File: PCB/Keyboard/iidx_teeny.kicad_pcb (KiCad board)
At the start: 2 copper layers, 150 x 100 mm, 46 parts, among them J1 CONN_01x05, SW1 SWITCH_SPST, SW10 SWITCH_SPST, SW11 SWITCH_SPST, SW12 SWITCH_SPST, SW13 SWITCH_SPST, SW2 SWITCH_SPST, SW3 SWITCH_SPST, SW4 SWITCH_SPST, SW5 SWITCH_SPST, SW6 SWITCH_SPST, SW7 SWITCH_SPST, SW8 SWITCH_SPST, SW9 SWITCH_SPST, U1 Pico, U2 SN74LV1T34DBV, U3 SN74LV1T34DBV

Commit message: PCB and keyboard housing done
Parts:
- removed TV1, TV2, TV3: D_TVS, Diode_SMD:D_SOD-323_HandSoldering
- added J2: Conn_01x04, iidx_teeny:Solder_4P, B.Cu at (138.4, 95.9)
- D1: renamed from D10; footprint iidx_pico:WS2812B-2835 -> iidx_teeny:WS2812B-2835
- D2: renamed from D20; footprint iidx_pico:WS2812B-2835 -> iidx_teeny:WS2812B-2835
- D3: renamed from D30; footprint iidx_pico:WS2812B-2835 -> iidx_teeny:WS2812B-2835
- D4: renamed from D40; footprint iidx_pico:WS2812B-2835 -> iidx_teeny:WS2812B-2835
- D5: renamed from D50; footprint iidx_pico:WS2812B-2835 -> iidx_teeny:WS2812B-2835
- D6: renamed from D60; footprint iidx_pico:WS2812B-2835 -> iidx_teeny:WS2812B-2835
- D7: renamed from D70; footprint iidx_pico:WS2812B-2835 -> iidx_teeny:WS2812B-2835
- DA1, DA2, DA3, DA4: footprint iidx_pico:WS2812B-2835 -> iidx_teeny:WS2812B-2835
- J1: value CONN_01x05 -> Conn_01x03; footprint iidx_pico:Pogo_5P_Female -> iidx_teeny:Solder_3P
- SCR1, SCR2, SCR3, SCR4: footprint iidx_pico:MountingHole_3.2mm_M3 -> iidx_teeny:MountingHole_3.2mm_M3
- U2, U3: footprint iidx_pico:SOT-23-5_Jumper -> iidx_teeny:SOT-23-5_Jumper
- moved C2 90.7 mm to (81.1, 127.7)
- moved J1 88.8 mm to (151.9, 95.9), turned to 90 degrees
- moved R3 78.9 mm to (150.9, 89.7), turned to 90 degrees
- moved U3 74.0 mm to (148.4, 89.4), turned to -90 degrees
- moved C5 63.2 mm to (176.9, 127.7)
- moved C3 39.9 mm to (104.9, 127.7)
- moved R20 25.8 mm to (137.1, 79.7)
- moved R21 25.8 mm to (140.1, 79.7)
- moved C1 18.3 mm to (138.3, 84.2), turned to -90 degrees
- moved R1 18.1 mm to (155.4, 89.7)
- moved C4 11.8 mm to (141.0, 127.7)
- moved U2 9.92 mm to (80.8, 110.9)
- moved R2 6.96 mm to (83.3, 111.2)
- moved DA1 0.50 mm to (83.3, 75.1)
- moved DA2 0.50 mm to (105.3, 75.1)
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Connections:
- J1 pad 1: GND -> +5V
- J1 pad 2: /SDA -> /TT_LED
- J1 pad 3: /SCL -> GND
- U1 pad 36: unconnected-(U1-Pad36) -> /3V3
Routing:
- net +5V: track 0.00 -> 517.4 mm, vias 0 -> 9
- net Net-(SW7-Pad1): track 0.00 -> 96.3 mm
- net /LED8: track 0.00 -> 85.7 mm, vias 0 -> 2
- net Net-(SW13-Pad1): track 0.00 -> 84.5 mm, vias 0 -> 1
- net Net-(SW12-Pad1): track 0.00 -> 81.1 mm, vias 0 -> 1
- net Net-(SW11-Pad1): track 0.00 -> 73.6 mm, vias 0 -> 1
- net Net-(SW6-Pad1): track 0.00 -> 65.6 mm, vias 0 -> 1
- net Net-(SW5-Pad1): track 0.00 -> 65.5 mm
- net /LED7: track 0.00 -> 61.7 mm
- net GND: track 0.00 -> 55.9 mm, vias 0 -> 16
- net /LED3: track 0.00 -> 54.8 mm
- net /LED5: track 0.00 -> 54.8 mm
- net /LED1: track 0.00 -> 54.8 mm
- net Net-(SW10-Pad1): track 0.00 -> 54.0 mm, vias 0 -> 1
- net Net-(SW3-Pad1): track 0.00 -> 53.1 mm
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- added copper zone on B.Cu, net GND
- added copper zone on F.Cu, net GND
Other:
- board text added: "3V C D G"
- board text added: "5V L G"
- board text removed: "G D C L V"

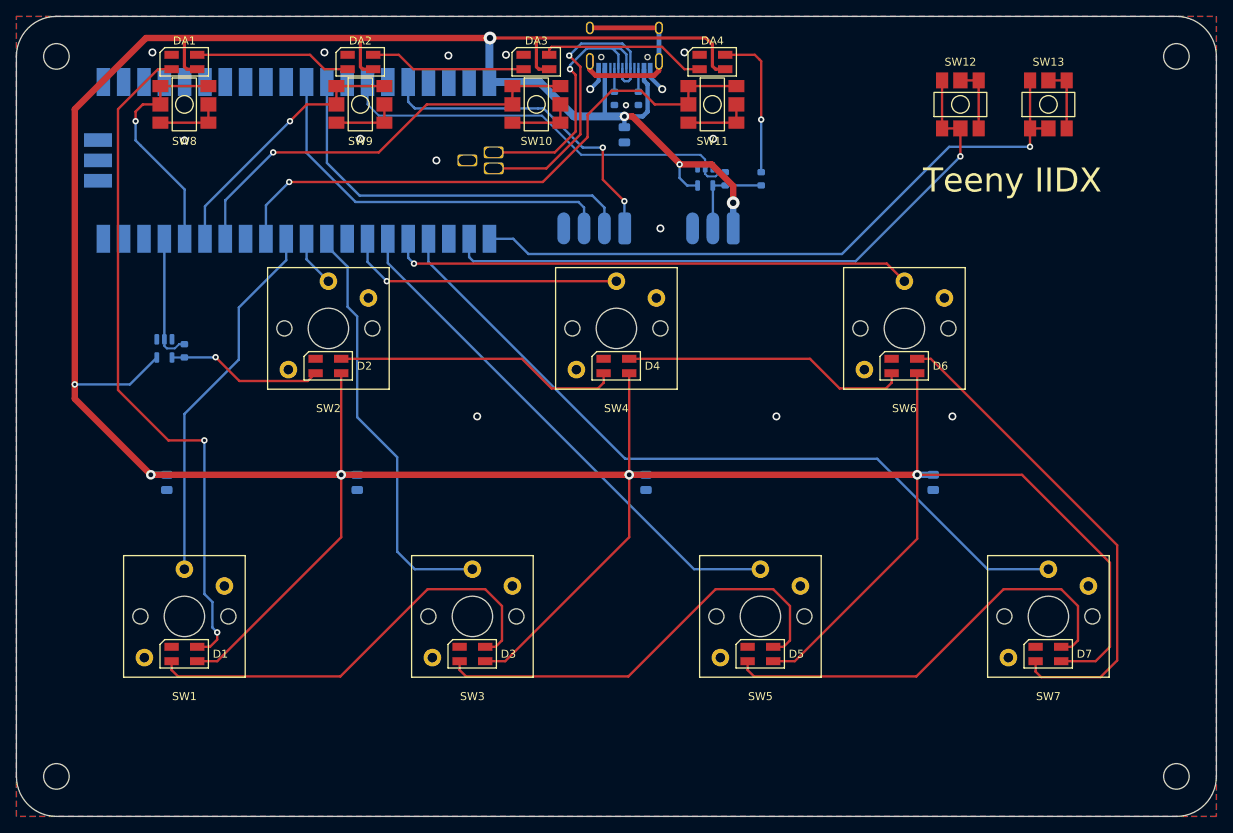
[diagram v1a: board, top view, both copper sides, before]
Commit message: PCB updated with two LEDs per button and larger Y gap
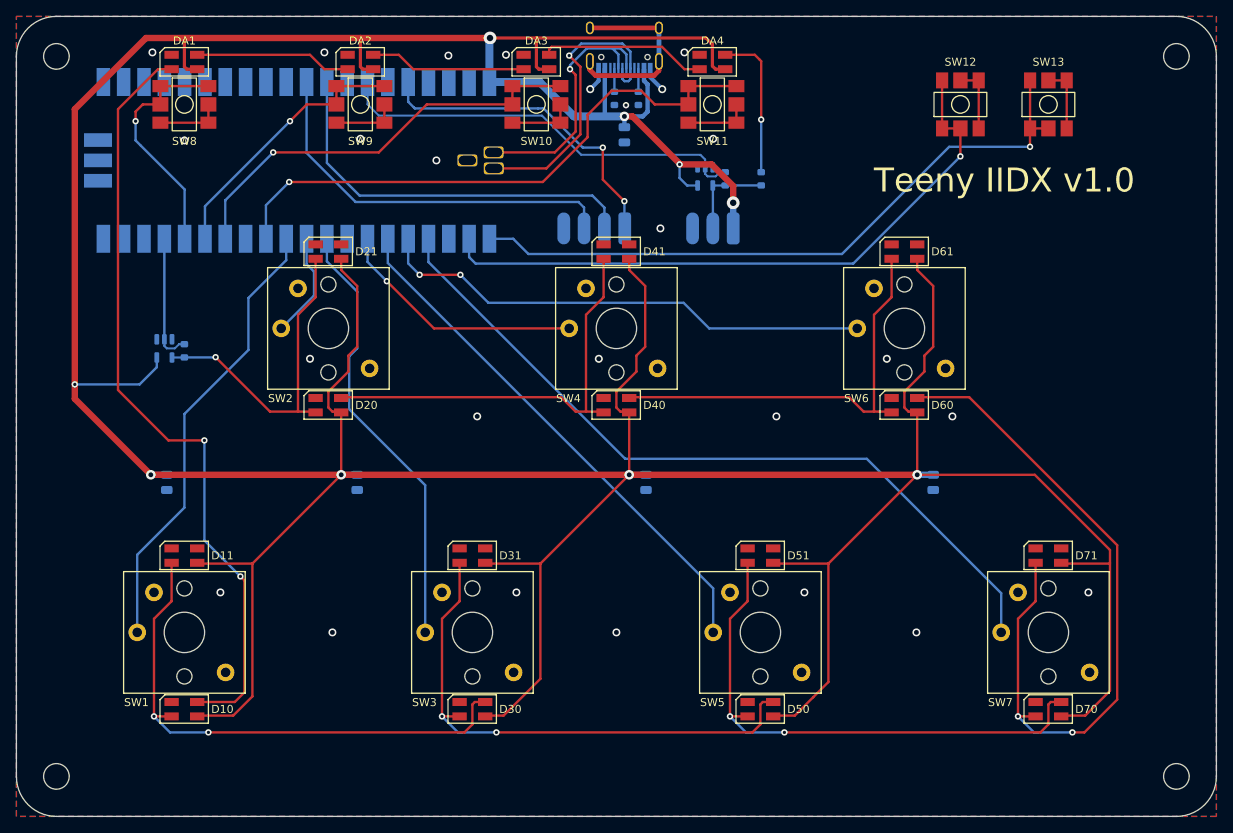
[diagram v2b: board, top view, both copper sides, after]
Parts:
- added D11: WS2812B_Unified, iidx_teeny:WS2812B-2835, F.Cu at (83.3, 136.8)
- added D21: WS2812B_Unified, iidx_teeny:WS2812B-2835, F.Cu at (101.3, 98.8)
- added D31: WS2812B_Unified, iidx_teeny:WS2812B-2835, F.Cu at (119.3, 136.8)
- added D41: WS2812B_Unified, iidx_teeny:WS2812B-2835, F.Cu at (137.3, 98.8)
- added D51: WS2812B_Unified, iidx_teeny:WS2812B-2835, F.Cu at (155.3, 136.8)
- added D61: WS2812B_Unified, iidx_teeny:WS2812B-2835, F.Cu at (173.3, 98.8)
- added D71: WS2812B_Unified, iidx_teeny:WS2812B-2835, F.Cu at (191.3, 136.8)
- moved D10 6.90 mm to (83.3, 156.0)
- moved D30 6.90 mm to (119.3, 156.0)
- moved D50 6.90 mm to (155.3, 156.0)
- moved D70 6.90 mm to (191.3, 156.0)
- moved D20 4.90 mm to (101.3, 118.0)
- moved D40 4.90 mm to (137.3, 118.0)
- moved D60 4.90 mm to (173.3, 118.0)
- moved SW1 2.00 mm to (83.3, 146.4), turned to 90 degrees
- moved SW3 2.00 mm to (119.3, 146.4), turned to 90 degrees
- moved SW5 2.00 mm to (155.3, 146.4), turned to 90 degrees
- moved SW7 2.00 mm to (191.3, 146.4), turned to 90 degrees
- turned SW2 to 90 degrees
- turned SW4 to 90 degrees
- turned SW6 to 90 degrees
- renumbered D1 to D10, D2 to D20, D3 to D30, D4 to D40, D5 to D50, D6 to D60, D7 to D70
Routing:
- net +5V: track 517.4 -> 626.8 mm
- net /LED7: track 61.7 -> 89.2 mm, vias 0 -> 2
- net /LED2: track 19.6 -> 40.8 mm
- net /LED6: track 35.8 -> 53.6 mm
- net /LED4: track 35.8 -> 53.6 mm
- net /LED1: track 54.8 -> 67.6 mm, vias 0 -> 2
- net /LED3: track 54.8 -> 67.6 mm, vias 0 -> 2
- net /LED5: track 54.8 -> 67.6 mm, vias 0 -> 2
- net /LED8: track 85.7 -> 97.2 mm
- net Net-(SW1-Pad1): track 46.6 -> 56.9 mm
- net Net-(SW2-Pad1): track 6.43 -> 13.3 mm
- net Net-(SW4-Pad1): track 35.0 -> 31.5 mm
- net Net-(SW6-Pad1): track 65.6 -> 62.6 mm, vias 1 -> 2
- net Net-(SW3-Pad1): track 53.1 -> 55.1 mm
- net Net-(SW5-Pad1): track 65.5 -> 66.0 mm
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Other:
- board text added: "Teeny IIDX v1.0"
- board text removed: "Teeny IIDX"

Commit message: Update USB-C position for stable cable connection
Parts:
- moved C1 2.00 mm to (138.3, 86.2)
- moved R20 2.00 mm to (137.1, 81.7)
- moved R21 2.00 mm to (140.1, 81.7)
- moved USB1 2.00 mm to (138.3, 70.2)
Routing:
- net Net-(U1-PadTP3): track 37.7 -> 35.1 mm
- net Net-(SW11-Pad1): track 73.6 -> 71.1 mm
- net Net-(R3-Pad2): track 52.5 -> 54.4 mm
- net Net-(U1-PadTP2): track 32.8 -> 31.3 mm
- net Net-(DA3-PadO): track 20.8 -> 19.5 mm
- net +5V: track 626.8 -> 627.7 mm
- net GND: vias 26 -> 27
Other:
- board text added: "Teeny IIDX v1.1"
- board text removed: "Teeny IIDX v1.0"

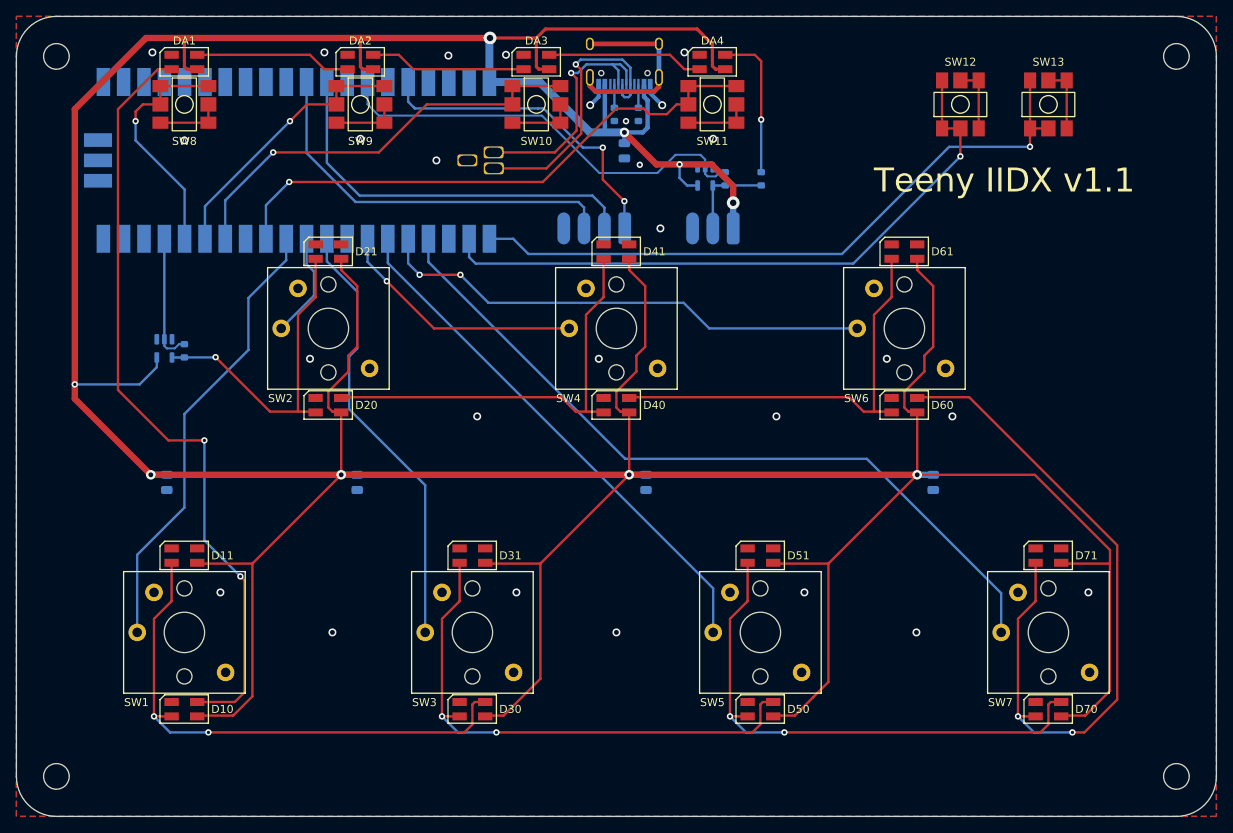
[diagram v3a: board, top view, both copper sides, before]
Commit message: PCB v1.2, easier soldering
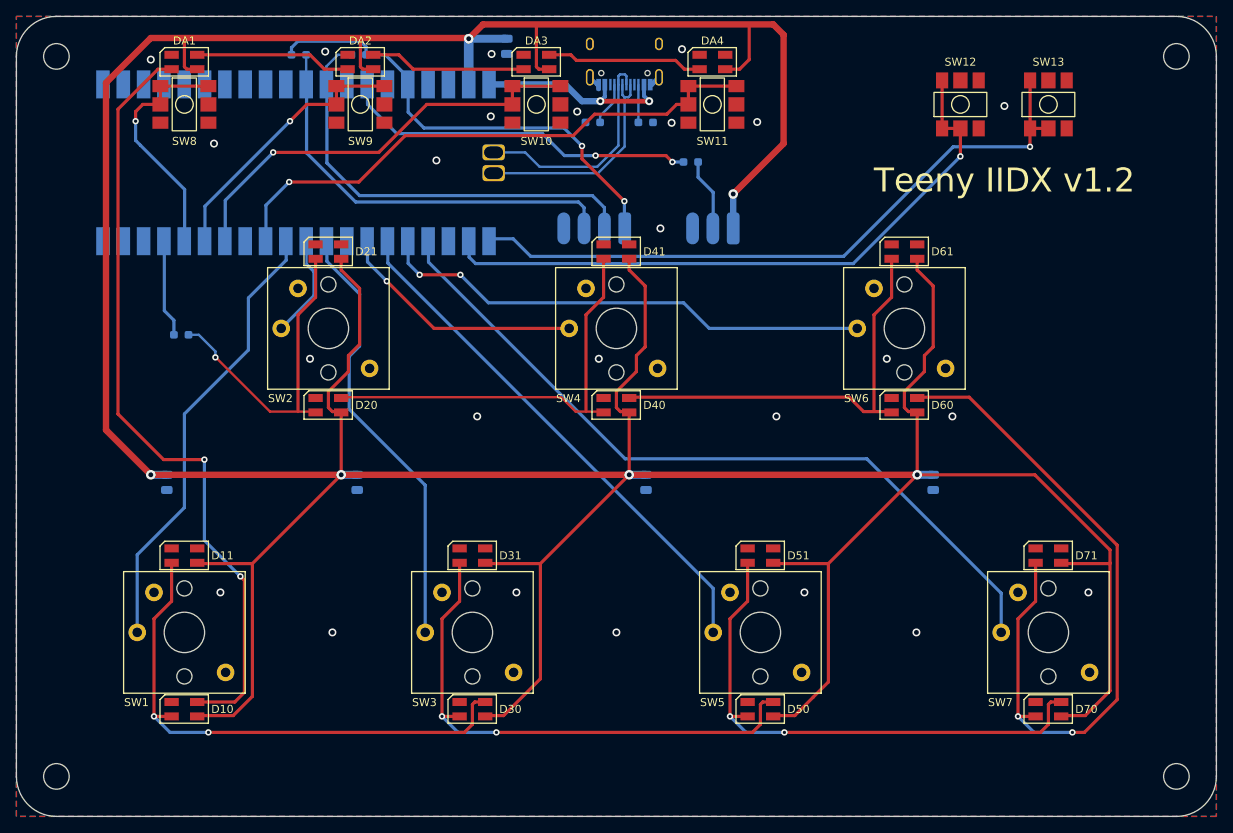
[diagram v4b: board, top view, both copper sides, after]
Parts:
- removed U2, U3: SN74LV1T34DBV, iidx_teeny:SOT-23-5_Jumper
- added R4: 10K, Resistor_SMD:R_0603_1608Metric_Pad0.98x0.95mm_HandSolder, B.Cu at (97.6, 74.2)
- R1, R2, R20, R21: footprint Resistor_SMD:R_0603_1608Metric -> Resistor_SMD:R_0603_1608Metric_Pad0.98x0.95mm_HandSolder
- R3: value 10 -> 10K; footprint Resistor_SMD:R_0603_1608Metric -> Resistor_SMD:R_0603_1608Metric_Pad0.98x0.95mm_HandSolder
- U1: value Pico -> PiPico_No_SWD; footprint iidx_teeny:RPi_Pico_SMD_Pins -> iidx_teeny:RPi_Pico_SMD_Pins_No_SWD_No_Text
- moved R1 75.1 mm to (82.9, 109.2), turned to 180 degrees
- moved R2 67.6 mm to (146.6, 87.6), turned to 180 degrees
- moved R3 48.4 mm to (105.1, 74.2), turned to 180 degrees
- moved C1 19.7 mm to (123.6, 73.1)
- moved R20 2.88 mm to (134.4, 82.7), turned to 180 degrees
- moved R21 1.35 mm to (141.0, 82.7), turned to 0 degrees
- moved U1 0.30 mm to (97.3, 87.7)
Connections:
- DA4 pad O: Net-(DA4-PadO) -> unconnected-(DA4-Out-PadO)
- R1 pad 1: Net-(DA4-PadO) -> /LED2
- R1 pad 2: /TT_LED -> Net-(U1-GPIO13)
- R2 pad 1: /LED2 -> /TT_LED
- R2 pad 2: Net-(R2-Pad2) -> Net-(U1-GPIO28_ADC2)
- R3 pad 1: /TT_LED -> /3V3
- R3 pad 2: Net-(R3-Pad2) -> /SCL
- U1 pad 17: Net-(R2-Pad2) -> Net-(U1-GPIO13)
- U1 pad 34: Net-(R3-Pad2) -> Net-(U1-GPIO28_ADC2)
- U1 pad 39: unconnected-(U1-Pad39) -> +5V
- U1 pad 40: +5V -> Net-(U1-VBUS)
- USB1 pad 11: +5V -> Net-(U1-VBUS)
- USB1 pad 13: unconnected-(USB1-Pad13) -> GND
- USB1 pad 2: +5V -> Net-(U1-VBUS)
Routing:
- net Net-(R3-Pad2): track 54.4 -> 0.00 mm
- net GND: track 55.9 -> 3.54 mm, vias 27 -> 25
- net Net-(U1-GPIO28_ADC2): track 0.00 -> 45.3 mm, vias 0 -> 2
- net +5V: track 627.7 -> 596.3 mm, vias 9 -> 6
- net Net-(U1-VBUS): track 0.00 -> 25.5 mm, vias 0 -> 2
- net unconnected-(USB1-Pad13): track 24.2 -> 0.00 mm
- net Net-(DA4-PadO): track 18.7 -> 0.00 mm, vias 1 -> 0
- net /3V3: track 40.4 -> 58.8 mm
- net Net-(R2-Pad2): track 16.2 -> 0.00 mm
- net Net-(U1-GPIO13): track 0.00 -> 12.5 mm
- net Net-(U1-USB2): track 35.1 -> 27.7 mm, vias 1 -> 0
- net /SCL: track 49.7 -> 55.7 mm
- net /SDA: track 49.0 -> 52.7 mm
- net Net-(U1-USB1): track 31.3 -> 28.4 mm, vias 1 -> 0
- net Net-(USB1-CC1): track 2.89 -> 5.46 mm
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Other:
- board text added: "Teeny IIDX v1.2"
- board text removed: "Teeny IIDX v1.1"

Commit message: PCB v1.3 (sensors on board)
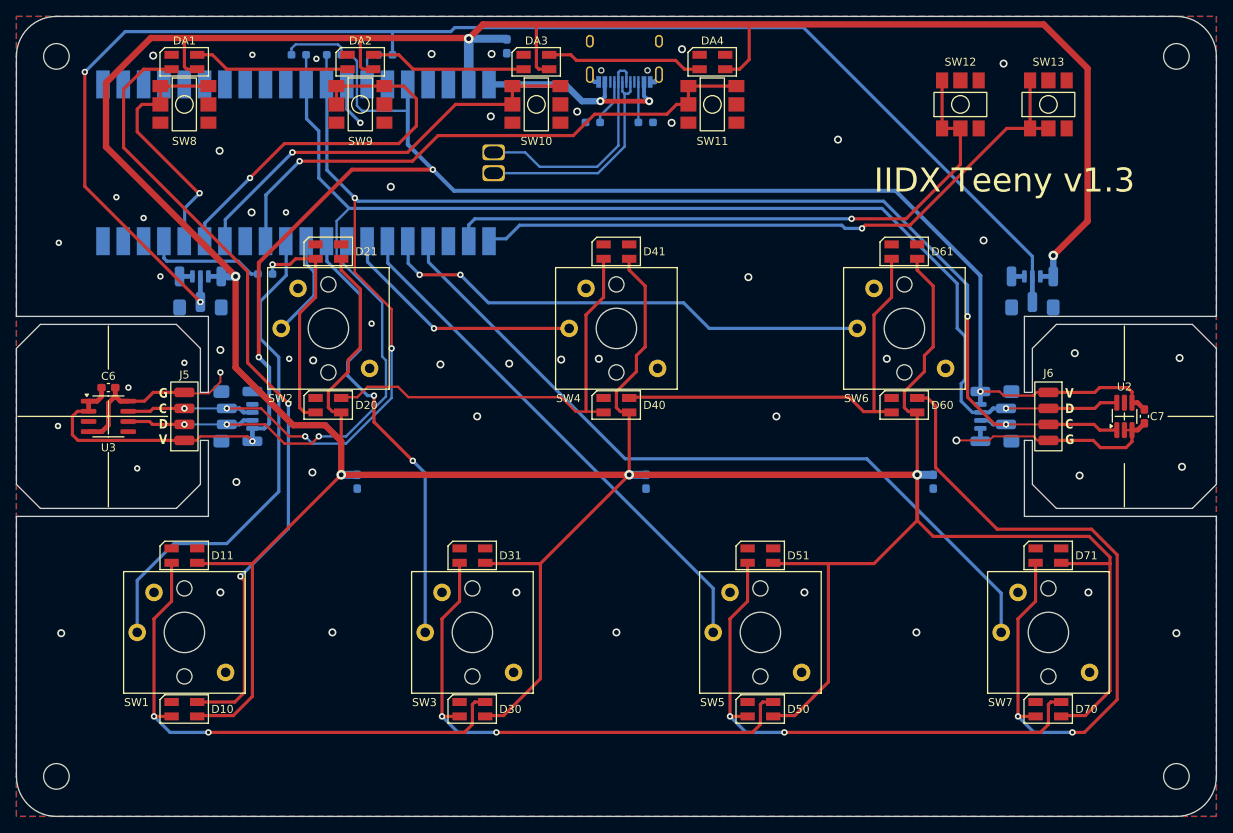
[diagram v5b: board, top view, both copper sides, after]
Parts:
- removed C5: 1uF, Capacitor_SMD:C_0805_2012Metric
- added C6: 1uF, Capacitor_SMD:C_0603_1608Metric_Pad1.08x0.95mm_HandSolder, F.Cu at (73.8, 115.8)
- added C7: 1uF, Capacitor_SMD:C_0603_1608Metric_Pad1.08x0.95mm_HandSolder, F.Cu at (203.3, 119.4)
- added J3: Spin, iidx_teeny:SH1.0_4P_Solder_Combo, B.Cu at (89.8, 119.4)
- added J4: Spin, iidx_teeny:SH1.0_4P_Solder_Combo, B.Cu at (184.8, 119.4)
- added J5: Spin, iidx_teeny:P2.0_4P_Solder, F.Cu at (83.3, 119.4)
- added J6: Spin, iidx_teeny:P2.0_4P_Solder, F.Cu at (191.3, 119.4)
- added U2: TMAG5273, Package_TO_SOT_SMD:TSOT-23-6_HandSoldering, F.Cu at (200.8, 119.4)
- added U3: AS5600, Package_SO:SOIC-8_3.9x4.9mm_P1.27mm, F.Cu at (73.8, 119.4)
- C1, C2, C3, C4: footprint Capacitor_SMD:C_0805_2012Metric -> Capacitor_SMD:C_0603_1608Metric_Pad1.08x0.95mm_HandSolder
- J1: value Conn_01x03 -> RGB; footprint iidx_teeny:Solder_3P -> iidx_teeny:SH1.0_3P_Solder_Combo
- J2: value Conn_01x04 -> RGB; footprint iidx_teeny:Solder_4P -> iidx_teeny:SH1.0_3P_Solder_Combo
- R3, R4: value 10K -> 5K1
- moved J1 67.1 mm to (85.3, 103.9), turned to 180 degrees
- moved J2 51.6 mm to (189.3, 103.9), turned to 180 degrees
- moved R2 40.5 mm to (108.4, 74.2)
- moved C3 36.1 mm to (141.0, 127.6)
- moved C4 35.9 mm to (176.9, 127.6)
- moved C2 23.8 mm to (104.9, 127.6)
- moved R1 13.0 mm to (93.4, 101.6)
- moved R3 3.08 mm to (102.0, 74.2)
- moved USB1 0.34 mm to (138.3, 69.9)
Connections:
- J2 pad 1: /3V3 -> +5V
- J2 pad 2: /SCL -> /TT_LED
- J2 pad 3: /SDA -> GND
- R3 pad 1: /3V3 -> +3.3V
- R4 pad 1: /3V3 -> +3.3V
- U1 pad 36: /3V3 -> +3.3V
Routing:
- net +3.3V: track 0.00 -> 231.1 mm, vias 0 -> 4
- net /TT_LED: track 9.10 -> 179.1 mm, vias 0 -> 2
- net /SDA: track 52.7 -> 203.8 mm, vias 0 -> 4
- net /SCL: track 55.7 -> 206.1 mm, vias 0 -> 7
- net GND: track 3.54 -> 63.9 mm, vias 25 -> 54
- net /3V3: track 58.8 -> 0.00 mm, vias 2 -> 0
- net Net-(U1-GPIO28_ADC2): track 45.3 -> 4.78 mm, vias 2 -> 0
- net +5V: track 596.3 -> 624.6 mm
- net Net-(U1-GPIO11): track 34.1 -> 49.8 mm
- net /LED2: track 40.3 -> 28.5 mm
- net Net-(U1-GPIO8): track 56.9 -> 62.7 mm
- net /LED7: track 89.2 -> 93.0 mm
- net Net-(U1-GPIO0): track 84.7 -> 81.9 mm
- net /LED8: track 97.6 -> 100.1 mm
- net Net-(U1-GPIO13): track 12.5 -> 14.7 mm
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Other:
- outline, holes or cut-outs redrawn
- board text added: "G C D V"
- board text added: "IIDX Teeny v1.3"
- board text added: "V D C G"
- board text removed: "3V C D G"
- board text removed: "5V L G"
- board text removed: "Teeny IIDX v1.2"
